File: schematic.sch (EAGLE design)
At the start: 88 parts, among them J1 MEGAFIT-4SKT-RA, J10 JST-PA-SMT-RA-4, J11 JST-PA-SMT-RA-2, J12 JST-PA-SMT-RA-2, J14 JST-PA-SMT-RA-2, J15 JST-PA-SMT-RA-2, J17 JST-PA-SMT-RA-3, J18 JST-PA-SMT-RA-3, J19 JST-PA-SMT-RA-4, J20 JST-PA-SMT-RA-4, J21 JST-PA-SMT-RA-3, J22 JST-PA-SMT-RA-3, J3 DF13-6, J4 DF13-5, J5 DF13-6, J6 SSW-116-02-S-TRA, J7 SSW-108-02-S-TRA, J8 SSW-108-02-S-D-RA, J9 SSW-106-02-S-D-RA, SW1 M2022LL2W13, SW2 M2022LL2W13, U1 VHE100W, U11 MED_MOSFET, U2 VHB150W, U4 INA139, U5 INA139, U6 INA139, U7 RELAY, U8 RELAY, U9 RELAY

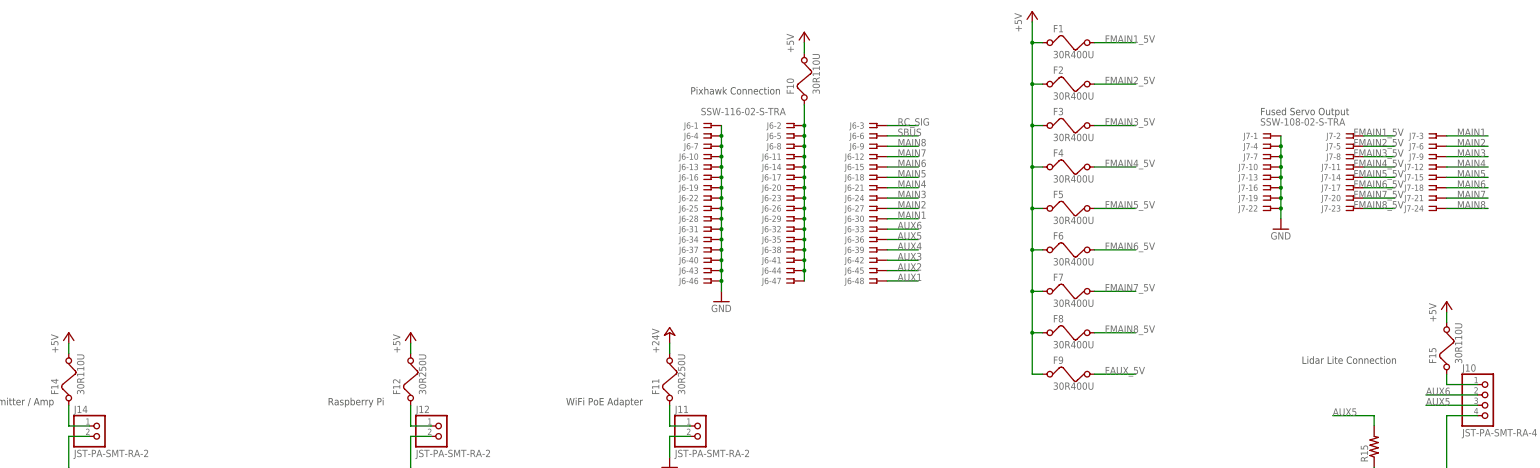
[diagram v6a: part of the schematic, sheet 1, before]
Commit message: Adding some 5v ptc smt devices instead of the big throughhole units.
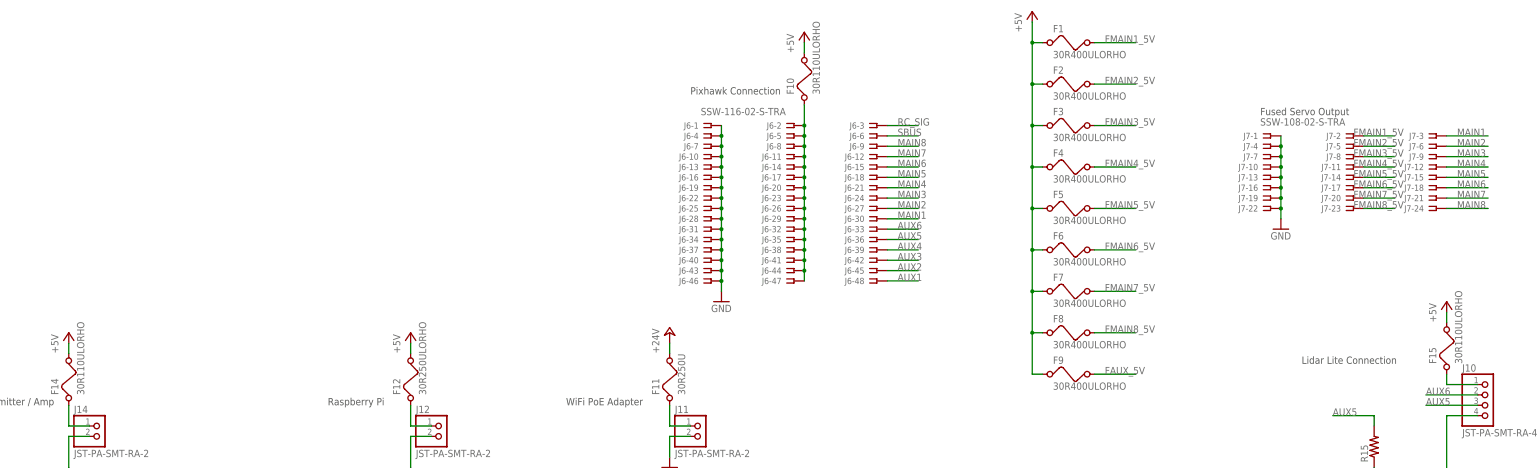
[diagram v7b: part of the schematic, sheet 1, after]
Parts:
- F1, F2, F3, F4, F5, F6, F7, F8, F9: value 30R400U -> 30R400ULORHO; device littelfuse:30R400U -> littelfuse:30R400ULORHO
- F10, F14, F15, F28, F29: value 30R110U -> 30R110ULORHO; device littelfuse:30R110U -> littelfuse:30R110ULORHO
- F12: value 30R250U -> 30R250ULORHO; device littelfuse:30R250U -> littelfuse:30R250ULORHO
- F30: value 30R160U -> 30R160ULORHO; device littelfuse:30R160U -> littelfuse:30R160ULORHO
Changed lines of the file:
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@@
 <grid distance="0.1" unitdist="inch" unit="inch" style="lines" multiple="1" display="no" altdistance="0.01" altunitdist="inch" altunit="inch"/>
 <layers>
-<layer number="1" name="Top" color="4" fill="1" visible="no" active="no"/>
-<layer number="2" name="Route2" color="1" fill="3" visible="no" active="no"/>
-<layer number="3" name="Route3" color="4" fill="3" visible="no" active="no"/>
-<layer number="14" name="Route14" color="1" fill="6" visible="no" active="no"/>
-<layer number="15" name="Route15" color="4" fill="6" visible="no" active="no"/>
-<layer number="16" name="Bottom" color="1" fill="1" visible="no" active="no"/>
-<layer number="17" name="Pads" color="2" fill="1" visible="no" active="no"/>
-<layer number="18" name="Vias" color="2" fill="1" visible="no" active="no"/>
-<layer number="19" name="Unrouted" color="6" fill="1" visible="no" active="no"/>
-<layer number="20" name="Dimension" color="15" fill="1" visible="no" active="no"/>
-<layer number="21" name="tPlace" color="7" fill="1" visible="no" active="no"/>
-<layer number="22" name="bPlace" color="7" fill="1" visible="no" active="no"/>
-<layer number="23" name="tOrigins" color="15" fill="1" visible="no" active="no"/>
-<layer number="24" name="bOrigins" color="15" fill="1" visible="no" active="no"/>
-<layer number="25" name="tNames" color="7" fill="1" visible="no" active="no"/>
-<layer number="26" name="bNames" color="7" fill="1" visible="no" active="no"/>
-<layer number="27" name="tValues" color="7" fill="1" visible="no" active="no"/>
-<layer number="28" name="bValues" color="7" fill="1" visible="no" active="no"/>
+<layer number="1" name="Top" color="4" fill="1" visible="yes" active="no"/>
+<layer number="2" name="Route2" color="1" fill="3" visible="yes" active="no"/>
+<layer number="3" name="Route3" color="4" fill="3" visible="yes" active="no"/>
+<layer number="14" name="Route14" color="1" fill="6" visible="yes" active="no"/>
+<layer number="15" name="Route15" color="4" fill="6" visible="yes" active="no"/>
+<layer number="16" name="Bottom" color="1" fill="1" visible="yes" active="no"/>
+<layer number="17" name="Pads" color="2" fill="1" visible="yes" active="no"/>
+<layer number="18" name="Vias" color="2" fill="1" visible="yes" active="no"/>
+<layer number="19" name="Unrouted" color="6" fill="1" visible="yes" active="no"/>
+<layer number="20" name="Dimension" color="15" fill="1" visible="yes" active="no"/>
+<layer number="21" name="tPlace" color="7" fill="1" visible="yes" active="no"/>
+<layer number="22" name="bPlace" color="7" fill="1" visible="yes" active="no"/>
+<layer number="23" name="tOrigins" color="15" fill="1" visible="yes" active="no"/>
+<layer number="24" name="bOrigins" color="15" fill="1" visible="yes" active="no"/>
+<layer number="25" name="tNames" color="7" fill="1" visible="yes" active="no"/>
+<layer number="26" name="bNames" color="7" fill="1" visible="yes" active="no"/>
+<layer number="27" name="tValues" color="7" fill="1" visible="yes" active="no"/>
+<layer number="28" name="bValues" color="7" fill="1" visible="yes" active="no"/>
 <layer number="29" name="tStop" color="7" fill="3" visible="no" active="no"/>
 <layer number="30" name="bStop" color="7" fill="6" visible="no" active="no"/>
@@
 <layer number="35" name="tGlue" color="7" fill="4" visible="no" active="no"/>
 <layer number="36" name="bGlue" color="7" fill="5" visible="no" active="no"/>
-<layer number="37" name="tTest" color="7" fill="1" visible="no" active="no"/>
-<layer number="38" name="bTest" color="7" fill="1" visible="no" active="no"/>
+<layer number="37" name="tTest" color="7" fill="1" visible="yes" active="no"/>
+<layer number="38" name="bTest" color="7" fill="1" visible="yes" active="no"/>
 <layer number="39" name="tKeepout" color="4" fill="11" visible="no" active="no"/>
 <layer number="40" name="bKeepout" color="1" fill="11" visible="no" active="no"/>
@@
 <layer number="44" name="Drills" color="7" fill="1" visible="no" active="no"/>
 <layer number="45" name="Holes" color="7" fill="1" visible="no" active="no"/>
-<layer number="46" name="Milling" color="3" fill="1" visible="no" active="no"/>
-<layer number="47" name="Measures" color="7" fill="1" visible="no" active="no"/>
-<layer number="48" name="Document" color="7" fill="1" visible="no" active="no"/>
-<layer number="49" name="Reference" color="7" fill="1" visible="no" active="no"/>
-<layer number="51" name="tDocu" color="6" fill="1" visible="no" active="no"/>
-<layer number="52" name="bDocu" color="7" fill="1" visible="no" active="no"/>
+<layer number="46" name="Milling" color="3" fill="1" visible="yes" active="no"/>
+<layer number="47" name="Measures" color="7" fill="1" visible="yes" active="no"/>
+<layer number="48" name="Document" color="7" fill="1" visible="yes" active="no"/>
+<layer number="49" name="Reference" color="7" fill="1" visible="yes" active="no"/>
+<layer number="51" name="tDocu" color="7" fill="1" visible="yes" active="no"/>
+<layer number="52" name="bDocu" color="7" fill="1" visible="yes" active="no"/>
 <layer number="90" name="Modules" color="5" fill="1" visible="yes" active="yes"/>
 <layer number="91" name="Nets" color="2" fill="1" visible="yes" active="yes"/>
@@
 <part name="J9" library="con-samtec" deviceset="SSW-106-02-S-D" device="-RA"/>
 <part name="U1" library="cui" deviceset="VHE100W" device=""/>
-<part name="F1" library="littelfuse" deviceset="30R400U" device=""/>
-<part name="F2" library="littelfuse" deviceset="30R400U" device=""/>
-<part name="F3" library="littelfuse" deviceset="30R400U" device=""/>
-<part name="F4" library="littelfuse" deviceset="30R400U" device=""/>
-<part name="F5" library="littelfuse" deviceset="30R400U" device=""/>
-<part name="F6" library="littelfuse" deviceset="30R400U" device=""/>
-<part name="F7" library="littelfuse" deviceset="30R400U" device=""/>
-<part name="F8" library="littelfuse" deviceset="30R400U" device=""/>
-<part name="F30" library="littelfuse" deviceset="30R160U" device=""/>
-<part name="F29" library="littelfuse" deviceset="30R110U" device=""/>
+<part name="F1" library="littelfuse" deviceset="30R400U" device="LORHO" value="30R400ULORHO"/>
+<part name="F2" library="littelfuse" deviceset="30R400U" device="LORHO" value="30R400ULORHO"/>
+<part name="F3" library="littelfuse" deviceset="30R400U" device="LORHO" value="30R400ULORHO"/>
+<part name="F4" library="littelfuse" deviceset="30R400U" device="LORHO" value="30R400ULORHO"/>
+<part name="F5" library="littelfuse" deviceset="30R400U" device="LORHO" value="30R400ULORHO"/>
+<part name="F6" library="littelfuse" deviceset="30R400U" device="LORHO" value="30R400ULORHO"/>
+<part name="F7" library="littelfuse" deviceset="30R400U" device="LORHO" value="30R400ULORHO"/>
+<part name="F8" library="littelfuse" deviceset="30R400U" device="LORHO" value="30R400ULORHO"/>
+<part name="F30" library="littelfuse" deviceset="30R160U" device="LORHO" value="30R160ULORHO"/>
+<part name="F29" library="littelfuse" deviceset="30R110U" device="LORHO" value="30R110ULORHO"/>
 <part name="J5" library="df13" deviceset="DF13-6" device=""/>
 <part name="P+2" library="supply1" deviceset="V+" device=""/>
@@
 <part name="GND7" library="supply1" deviceset="GND" device=""/>
 <part name="P+7" library="supply1" deviceset="+5V" device=""/>
-<part name="F9" library="littelfuse" deviceset="30R400U" device=""/>
+<part name="F9" library="littelfuse" deviceset="30R400U" device="LORHO" value="30R400ULORHO"/>
 <part name="P+8" library="supply1" deviceset="+5V" device=""/>
-<part name="F10" library="littelfuse" deviceset="30R110U" device=""/>
+<part name="F10" library="littelfuse" deviceset="30R110U" device="LORHO" value="30R110ULORHO"/>
 <part name="P+9" library="supply1" deviceset="+5V" device=""/>
 <part name="GND9" library="supply1" deviceset="GND" device=""/>
@@
 <part name="J3" library="df13" deviceset="DF13-6" device=""/>
 <part name="GND12" library="supply1" deviceset="GND" device=""/>
-<part name="F28" library="littelfuse" deviceset="30R110U" device=""/>
+<part name="F28" library="littelfuse" deviceset="30R110U" device="LORHO" value="30R110ULORHO"/>
 <part name="P+11" library="supply1" deviceset="+5V" device=""/>
 <part name="F11" library="littelfuse" deviceset="30R250U" device=""/>
@@
 <part name="GND27" library="supply1" deviceset="GND" device=""/>
 <part name="GND28" library="supply1" deviceset="GND" device=""/>
-<part name="F12" library="littelfuse" deviceset="30R250U" device=""/>
+<part name="F12" library="littelfuse" deviceset="30R250U" device="LORHO" value="30R250ULORHO"/>
 <part name="GND29" library="supply1" deviceset="GND" device=""/>
 <part name="P+17" library="supply1" deviceset="+5V" device=""/>
@@
 <part name="R15" library="rcl" deviceset="R-US_" device="M0805"/>
 <part name="GND30" library="supply1" deviceset="GND" device=""/>
-<part name="F15" library="littelfuse" deviceset="30R110U" device=""/>
+<part name="F15" library="littelfuse" deviceset="30R110U" device="LORHO" value="30R110ULORHO"/>
 <part name="P+31" library="supply1" deviceset="+5V" device=""/>
 <part name="U2" library="cui" deviceset="VHB150W" device=""/>
 <part name="GND35" library="supply1" deviceset="GND" device=""/>
 <part name="P+25" library="supply1" deviceset="+5V" device=""/>
-<part name="F14" library="littelfuse" deviceset="30R110U" device=""/>
+<part name="F14" library="littelfuse" deviceset="30R110U" device="LORHO" value="30R110ULORHO"/>
 <part name="GND36" library="supply1" deviceset="GND" device=""/>
 <part name="GND37" library="supply1" deviceset="GND" device=""/>

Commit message: Updated so all fuses are SMT.
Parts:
- removed F9: 30R400ULORHO, littelfuse:30R400ULORHO
- F11: value 30R250U -> 30R110U2920L; device littelfuse:30R250U -> littelfuse:30R110U2920L
- F16: value 30R250U -> 30R250U2920L; device littelfuse:30R250U -> littelfuse:30R250U2920L
- F18, F19, F21, F23: value 30R160U -> 30R160U2920L; device littelfuse:30R160U -> littelfuse:30R160U2920L
- F20, F22, F24, F25, F26, F27: value 30R110U -> 30R110U2920L; device littelfuse:30R110U -> littelfuse:30R110U2920L
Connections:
- removed net FAUX_5V: F9.2
- net +5V: no longer F9.1
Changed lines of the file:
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@@
 <part name="GND7" library="supply1" deviceset="GND" device=""/>
 <part name="P+7" library="supply1" deviceset="+5V" device=""/>
-<part name="F9" library="littelfuse" deviceset="30R400U" device="LORHO" value="30R400ULORHO"/>
 <part name="P+8" library="supply1" deviceset="+5V" device=""/>
 <part name="F10" library="littelfuse" deviceset="30R110U" device="LORHO" value="30R110ULORHO"/>
@@
 <part name="F28" library="littelfuse" deviceset="30R110U" device="LORHO" value="30R110ULORHO"/>
 <part name="P+11" library="supply1" deviceset="+5V" device=""/>
-<part name="F11" library="littelfuse" deviceset="30R250U" device=""/>
 <part name="P+12" library="supply1" deviceset="+24V" device=""/>
 <part name="GND13" library="supply1" deviceset="GND" device=""/>
@@
 <part name="GND29" library="supply1" deviceset="GND" device=""/>
 <part name="P+17" library="supply1" deviceset="+5V" device=""/>
-<part name="F16" library="littelfuse" deviceset="30R250U" device=""/>
+<part name="F16" library="littelfuse" deviceset="30R250U" device="2920L" value="30R250U2920L"/>
 <part name="P+28" library="supply1" deviceset="+24V" device=""/>
 <part name="JP1" library="pinhead" deviceset="PINHD-1X3" device=""/>
@@
 <part name="P+36" library="supply1" deviceset="+5V" device=""/>
 <part name="U8" library="pololu" deviceset="RELAY" device=""/>
-<part name="F21" library="littelfuse" deviceset="30R160U" device=""/>
-<part name="F23" library="littelfuse" deviceset="30R160U" device=""/>
+<part name="F21" library="littelfuse" deviceset="30R160U" device="2920L" value="30R160U2920L"/>
+<part name="F23" library="littelfuse" deviceset="30R160U" device="2920L" value="30R160U2920L"/>
 <part name="P+4" library="supply1" deviceset="+24V" device=""/>
 <part name="GND1" library="supply1" deviceset="GND" device=""/>
 <part name="P+14" library="supply1" deviceset="+5V" device=""/>
 <part name="U9" library="pololu" deviceset="RELAY" device=""/>
-<part name="F18" library="littelfuse" deviceset="30R160U" device=""/>
-<part name="F19" library="littelfuse" deviceset="30R160U" device=""/>
+<part name="F18" library="littelfuse" deviceset="30R160U" device="2920L" value="30R160U2920L"/>
+<part name="F19" library="littelfuse" deviceset="30R160U" device="2920L" value="30R160U2920L"/>
 <part name="GND31" library="supply1" deviceset="GND" device=""/>
 <part name="GND39" library="supply1" deviceset="GND" device=""/>
 <part name="GND40" library="supply1" deviceset="GND" device=""/>
 <part name="GND41" library="supply1" deviceset="GND" device=""/>
-<part name="F24" library="littelfuse" deviceset="30R110U" device=""/>
-<part name="F25" library="littelfuse" deviceset="30R110U" device=""/>
-<part name="F27" library="littelfuse" deviceset="30R110U" device=""/>
-<part name="F26" library="littelfuse" deviceset="30R110U" device=""/>
-<part name="F22" library="littelfuse" deviceset="30R110U" device=""/>
-<part name="F20" library="littelfuse" deviceset="30R110U" device=""/>
+<part name="F24" library="littelfuse" deviceset="30R110U" device="2920L" value="30R110U2920L"/>
+<part name="F25" library="littelfuse" deviceset="30R110U" device="2920L" value="30R110U2920L"/>
+<part name="F27" library="littelfuse" deviceset="30R110U" device="2920L" value="30R110U2920L"/>
+<part name="F26" library="littelfuse" deviceset="30R110U" device="2920L" value="30R110U2920L"/>
+<part name="F22" library="littelfuse" deviceset="30R110U" device="2920L" value="30R110U2920L"/>
+<part name="F20" library="littelfuse" deviceset="30R110U" device="2920L" value="30R110U2920L"/>
 <part name="J7" library="con-samtec" deviceset="SSW-108-02-S-T" device="RA"/>
 <part name="GND15" library="supply1" deviceset="GND" device=""/>
@@
 <part name="J20" library="jst" deviceset="JST-PA-SMT-RA-4" device=""/>
 <part name="J10" library="jst" deviceset="JST-PA-SMT-RA-4" device=""/>
+<part name="F11" library="littelfuse" deviceset="30R110U" device="2920L" value="30R110U2920L"/>
 </parts>
 <sheets>
@@
 <instance part="F8" gate="G$1" x="172.72" y="-12.7"/>
 <instance part="GND7" gate="1" x="86.36" y="-5.08"/>
-<instance part="F9" gate="G$1" x="172.72" y="-22.86"/>
 <instance part="P+8" gate="1" x="162.56" y="66.04"/>
 <instance part="F10" gate="G$1" x="106.68" y="50.8" rot="R90"/>
 <instance part="P+9" gate="1" x="106.68" y="60.96"/>
-<instance part="F11" gate="G$1" x="73.66" y="-22.86" rot="R90"/>
 <instance part="P+12" gate="1" x="73.66" y="-12.7"/>
 <instance part="GND13" gate="1" x="73.66" y="-45.72"/>
@@
 <instance part="J20" gate="G$1" x="-35.56" y="-165.1"/>
 <instance part="J10" gate="G$1" x="271.78" y="-27.94"/>
+<instance part="F11" gate="G$1" x="73.66" y="-22.86" rot="R90"/>
 </instances>
 <busses>
@@
 <net name="+24V" class="0">
 <segment>
-<pinref part="F11" gate="G$1" pin="2"/>
 <pinref part="P+12" gate="1" pin="+24V"/>
 <wire x1="73.66" y1="-15.24" x2="73.66" y2="-17.78" width="0.1524" layer="91"/>
+<pinref part="F11" gate="G$1" pin="2"/>
 </segment>
 <segment>
@@
 <wire x1="162.56" y1="-12.7" x2="162.56" y2="-2.54" width="0.1524" layer="91"/>
 <junction x="162.56" y="-2.54"/>
-<pinref part="F9" gate="G$1" pin="1"/>
-<wire x1="165.1" y1="-22.86" x2="162.56" y2="-22.86" width="0.1524" layer="91"/>
-<wire x1="162.56" y1="-22.86" x2="162.56" y2="-12.7" width="0.1524" layer="91"/>
-<junction x="162.56" y="-12.7"/>
 </segment>
 <segment>
@@
 <wire x1="243.84" y1="17.78" x2="251.46" y2="17.78" width="0.1524" layer="91"/>
 <label x="241.3" y="17.78" size="1.778" layer="95"/>
-</segment>
-</net>
-<net name="FAUX_5V" class="0">
-<segment>
-<pinref part="F9" gate="G$1" pin="2"/>
-<wire x1="177.8" y1="-22.86" x2="187.96" y2="-22.86" width="0.1524" layer="91"/>
-<label x="180.34" y="-22.86" size="1.778" layer="95"/>
 </segment>
 </net>
@@
 <net name="N$10" class="0">
 <segment>
-<pinref part="F11" gate="G$1" pin="1"/>
 <wire x1="73.66" y1="-30.48" x2="73.66" y2="-35.56" width="0.1524" layer="91"/>
 <wire x1="73.66" y1="-35.56" x2="78.74" y2="-35.56" width="0.1524" layer="91"/>
 <pinref part="J11" gate="G$1" pin="1"/>
-</segment>
-</net>
+<pinref part="F11" gate="G$1" pin="1"/>
+</segment>
+</net>
